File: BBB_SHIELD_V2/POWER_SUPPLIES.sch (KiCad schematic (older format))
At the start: 16 parts, among them P12V1 VX78XX, P5V1 VX78XX

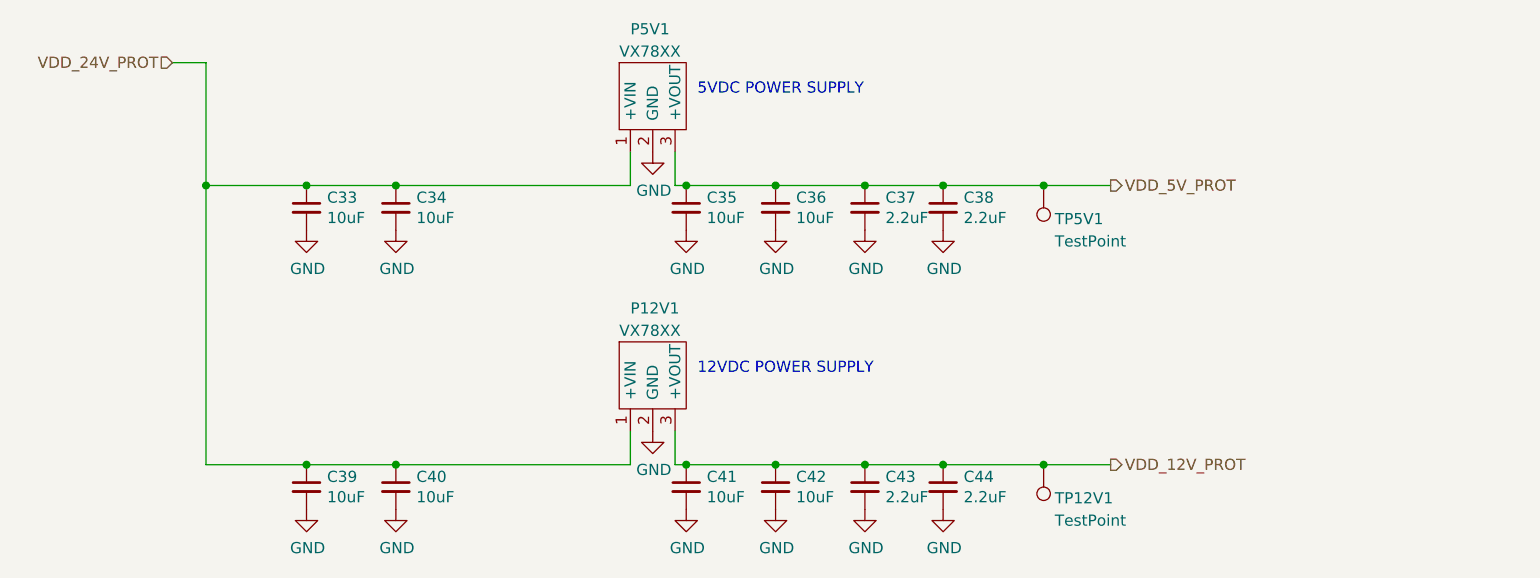
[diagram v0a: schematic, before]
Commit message: Cleaned up schematic.
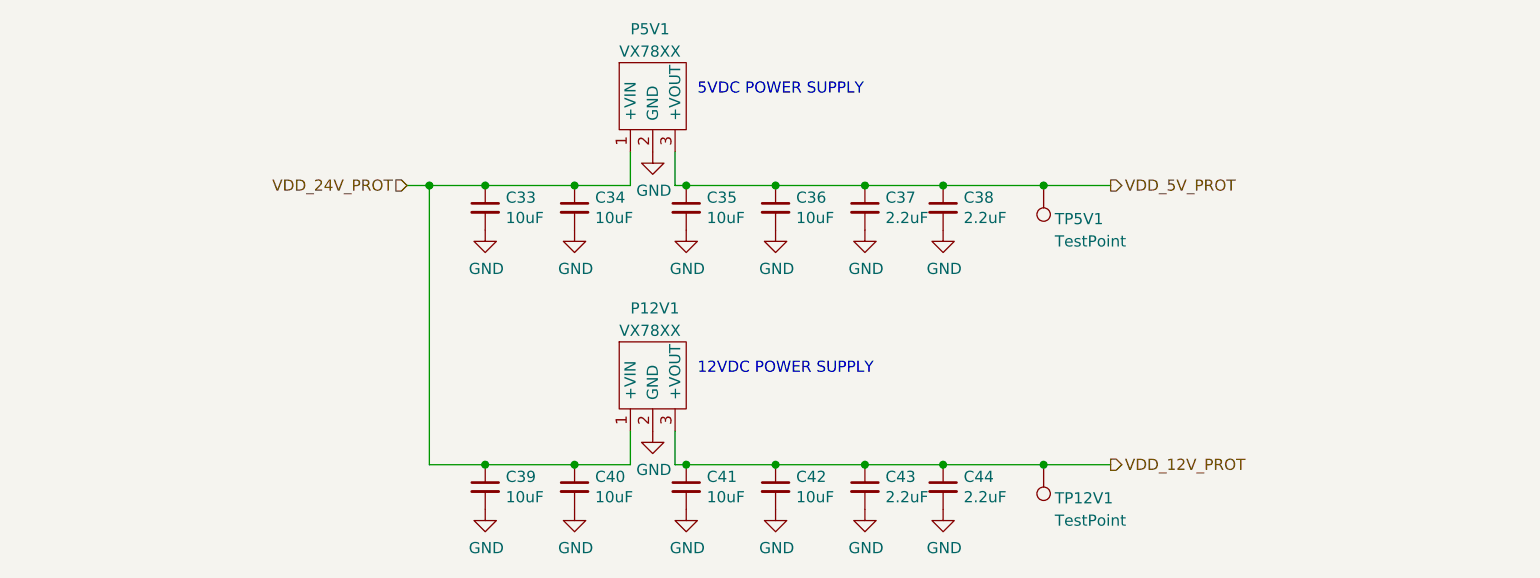
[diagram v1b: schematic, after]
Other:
- moved on the sheet: C33, C34, C39, C40
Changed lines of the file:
@@
 	1    0    0    -1
 $EndComp
-Text HLabel 1800 2200 0    50   Input ~ 0
+Text HLabel 2850 2750 0    50   Input ~ 0
 VDD_24V_PROT
 Text HLabel 6000 2750 2    50   Output ~ 0
@@
 	3850 2600 3850 2750
 Wire Wire Line
-	1950 2750 1950 2200
-Wire Wire Line
-	1950 2200 1800 2200
-Wire Wire Line
 	3850 3850 3850 4000
-Wire Wire Line
-	1950 4000 1950 2750
-Connection ~ 1950 2750
 $Comp
 L power:GND #PWR058
@@
 L Device:C_Small C33
 U 1 1 5C3C2F7D
-P 2400 2850
-F 0 "C33" H 2492 2896 50  0000 L CNN
-F 1 "10uF" H 2492 2805 50  0000 L CNN
-F 2 "Capacitor_SMD:C_1206_3216Metric" H 2400 2850 50  0001 C CNN
-F 3 "~" H 2400 2850 50  0001 C CNN
-F 4 "1276-6736-1-ND" H 2400 2850 50  0001 C CNN "DKPN"
-F 5 "CL31A106MBHNNNE" H 2400 2850 50  0001 C CNN "MFGPN"
-F 6 "X5R" H 2400 2850 50  0001 C CNN "TCO"
-F 7 "50" H 2400 2850 50  0001 C CNN "VOLTAGE"
-	1    2400 2850
-	1    0    0    -1
-$EndComp
-Connection ~ 2400 2750
-Wire Wire Line
-	2400 2750 1950 2750
+P 3200 2850
+F 0 "C33" H 3292 2896 50  0000 L CNN
+F 1 "10uF" H 3292 2805 50  0000 L CNN
+F 2 "Capacitor_SMD:C_1206_3216Metric" H 3200 2850 50  0001 C CNN
+F 3 "~" H 3200 2850 50  0001 C CNN
+F 4 "1276-6736-1-ND" H 3200 2850 50  0001 C CNN "DKPN"
+F 5 "CL31A106MBHNNNE" H 3200 2850 50  0001 C CNN "MFGPN"
+F 6 "X5R" H 3200 2850 50  0001 C CNN "TCO"
+F 7 "50" H 3200 2850 50  0001 C CNN "VOLTAGE"
+	1    3200 2850
+	1    0    0    -1
+$EndComp
 $Comp
 L power:GND #PWR056
 U 1 1 5C3C3A06
-P 2400 2950
-F 0 "#PWR056" H 2400 2700 50  0001 C CNN
-F 1 "GND" H 2405 2777 50  0000 C CNN
-F 2 "" H 2400 2950 50  0001 C CNN
-F 3 "" H 2400 2950 50  0001 C CNN
-	1    2400 2950
+P 3200 2950
+F 0 "#PWR056" H 3200 2700 50  0001 C CNN
+F 1 "GND" H 3205 2777 50  0000 C CNN
+F 2 "" H 3200 2950 50  0001 C CNN
+F 3 "" H 3200 2950 50  0001 C CNN
+	1    3200 2950
 	1    0    0    -1
 $EndComp
@@
 L power:GND #PWR057
 U 1 1 5C3C3A58
-P 2800 2950
-F 0 "#PWR057" H 2800 2700 50  0001 C CNN
-F 1 "GND" H 2805 2777 50  0000 C CNN
-F 2 "" H 2800 2950 50  0001 C CNN
-F 3 "" H 2800 2950 50  0001 C CNN
-	1    2800 2950
+P 3600 2950
+F 0 "#PWR057" H 3600 2700 50  0001 C CNN
+F 1 "GND" H 3605 2777 50  0000 C CNN
+F 2 "" H 3600 2950 50  0001 C CNN
+F 3 "" H 3600 2950 50  0001 C CNN
+	1    3600 2950
 	1    0    0    -1
 $EndComp
@@
 L power:GND #PWR063
 U 1 1 5C3C3AE4
-P 2400 4200
-F 0 "#PWR063" H 2400 3950 50  0001 C CNN
-F 1 "GND" H 2405 4027 50  0000 C CNN
-F 2 "" H 2400 4200 50  0001 C CNN
-F 3 "" H 2400 4200 50  0001 C CNN
-	1    2400 4200
+P 3200 4200
+F 0 "#PWR063" H 3200 3950 50  0001 C CNN
+F 1 "GND" H 3205 4027 50  0000 C CNN
+F 2 "" H 3200 4200 50  0001 C CNN
+F 3 "" H 3200 4200 50  0001 C CNN
+	1    3200 4200
 	1    0    0    -1
 $EndComp
@@
 L power:GND #PWR064
 U 1 1 5C3C3B36
-P 2800 4200
-F 0 "#PWR064" H 2800 3950 50  0001 C CNN
-F 1 "GND" H 2805 4027 50  0000 C CNN
-F 2 "" H 2800 4200 50  0001 C CNN
-F 3 "" H 2800 4200 50  0001 C CNN
-	1    2800 4200
+P 3600 4200
+F 0 "#PWR064" H 3600 3950 50  0001 C CNN
+F 1 "GND" H 3605 4027 50  0000 C CNN
+F 2 "" H 3600 4200 50  0001 C CNN
+F 3 "" H 3600 4200 50  0001 C CNN
+	1    3600 4200
 	1    0    0    -1
 $EndComp
@@
 	5250 4000 5700 4000
 Wire Wire Line
-	2400 2750 2800 2750
-Wire Wire Line
 	4050 2750 4100 2750
 Wire Wire Line
 	4050 4000 4100 4000
-Wire Wire Line
-	1950 4000 2400 4000
 $Comp
 L Device:C_Small C34
 U 1 1 5D1133B6
-P 2800 2850
-F 0 "C34" H 2892 2896 50  0000 L CNN
-F 1 "10uF" H 2892 2805 50  0000 L CNN
-F 2 "Capacitor_SMD:C_1206_3216Metric" H 2800 2850 50  0001 C CNN
-F 3 "~" H 2800 2850 50  0001 C CNN
-F 4 "1276-6736-1-ND" H 2800 2850 50  0001 C CNN "DKPN"
-F 5 "CL31A106MBHNNNE" H 2800 2850 50  0001 C CNN "MFGPN"
-F 6 "X5R" H 2800 2850 50  0001 C CNN "TCO"
-F 7 "50" H 2800 2850 50  0001 C CNN "VOLTAGE"
-	1    2800 2850
+P 3600 2850
+F 0 "C34" H 3692 2896 50  0000 L CNN
+F 1 "10uF" H 3692 2805 50  0000 L CNN
+F 2 "Capacitor_SMD:C_1206_3216Metric" H 3600 2850 50  0001 C CNN
+F 3 "~" H 3600 2850 50  0001 C CNN
+F 4 "1276-6736-1-ND" H 3600 2850 50  0001 C CNN "DKPN"
+F 5 "CL31A106MBHNNNE" H 3600 2850 50  0001 C CNN "MFGPN"
+F 6 "X5R" H 3600 2850 50  0001 C CNN "TCO"
+F 7 "50" H 3600 2850 50  0001 C CNN "VOLTAGE"
+	1    3600 2850
 	1    0    0    -1
 $EndComp
@@
 L Device:C_Small C39
 U 1 1 5D1136C3
-P 2400 4100
-F 0 "C39" H 2492 4146 50  0000 L CNN
-F 1 "10uF" H 2492 4055 50  0000 L CNN
-F 2 "Capacitor_SMD:C_1206_3216Metric" H 2400 4100 50  0001 C CNN
-F 3 "~" H 2400 4100 50  0001 C CNN
-F 4 "1276-6736-1-ND" H 2400 4100 50  0001 C CNN "DKPN"
-F 5 "CL31A106MBHNNNE" H 2400 4100 50  0001 C CNN "MFGPN"
-F 6 "X5R" H 2400 4100 50  0001 C CNN "TCO"
-F 7 "50" H 2400 4100 50  0001 C CNN "VOLTAGE"
-	1    2400 4100
+P 3200 4100
+F 0 "C39" H 3292 4146 50  0000 L CNN
+F 1 "10uF" H 3292 4055 50  0000 L CNN
+F 2 "Capacitor_SMD:C_1206_3216Metric" H 3200 4100 50  0001 C CNN
+F 3 "~" H 3200 4100 50  0001 C CNN
+F 4 "1276-6736-1-ND" H 3200 4100 50  0001 C CNN "DKPN"
+F 5 "CL31A106MBHNNNE" H 3200 4100 50  0001 C CNN "MFGPN"
+F 6 "X5R" H 3200 4100 50  0001 C CNN "TCO"
+F 7 "50" H 3200 4100 50  0001 C CNN "VOLTAGE"
+	1    3200 4100
 	1    0    0    -1
 $EndComp
@@
 L Device:C_Small C40
 U 1 1 5D1137C0
-P 2800 4100
-F 0 "C40" H 2892 4146 50  0000 L CNN
-F 1 "10uF" H 2892 4055 50  0000 L CNN
-F 2 "Capacitor_SMD:C_1206_3216Metric" H 2800 4100 50  0001 C CNN
-F 3 "~" H 2800 4100 50  0001 C CNN
-F 4 "1276-6736-1-ND" H 2800 4100 50  0001 C CNN "DKPN"
-F 5 "CL31A106MBHNNNE" H 2800 4100 50  0001 C CNN "MFGPN"
-F 6 "X5R" H 2800 4100 50  0001 C CNN "TCO"
-F 7 "50" H 2800 4100 50  0001 C CNN "VOLTAGE"
-	1    2800 4100
+P 3600 4100
+F 0 "C40" H 3692 4146 50  0000 L CNN
+F 1 "10uF" H 3692 4055 50  0000 L CNN
+F 2 "Capacitor_SMD:C_1206_3216Metric" H 3600 4100 50  0001 C CNN
+F 3 "~" H 3600 4100 50  0001 C CNN
+F 4 "1276-6736-1-ND" H 3600 4100 50  0001 C CNN "DKPN"
+F 5 "CL31A106MBHNNNE" H 3600 4100 50  0001 C CNN "MFGPN"
+F 6 "X5R" H 3600 4100 50  0001 C CNN "TCO"
+F 7 "50" H 3600 4100 50  0001 C CNN "VOLTAGE"
+	1    3600 4100
 	1    0    0    -1
 $EndComp
@@
 Wire Wire Line
 	4100 4000 4500 4000
-Connection ~ 2800 4000
-Wire Wire Line
-	2800 4000 3850 4000
-Connection ~ 2400 4000
-Wire Wire Line
-	2400 4000 2800 4000
-Connection ~ 2800 2750
-Wire Wire Line
-	2800 2750 3850 2750
 Connection ~ 4100 2750
 Wire Wire Line
@@
 Wire Wire Line
 	5700 4000 6000 4000
+Wire Wire Line
+	3200 2750 3600 2750
+Connection ~ 3600 2750
+Wire Wire Line
+	3600 2750 3850 2750
+Wire Wire Line
+	3200 4000 3600 4000
+Connection ~ 3600 4000
+Wire Wire Line
+	3600 4000 3850 4000
+Wire Wire Line
+	3200 2750 2950 2750
+Connection ~ 3200 2750
+Wire Wire Line
+	3200 4000 2950 4000
+Connection ~ 3200 4000
+Wire Wire Line
+	2950 2750 2950 4000
+Wire Wire Line
+	2850 2750 2950 2750
+Connection ~ 2950 2750
 $EndSCHEMATC

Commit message: Rev 2 problem fixes.
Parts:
- added C46, C47, C48: 180uF,50V, Capacitor_THT:CP_Radial_D8.0mm_P3.50mm, symbol Device:CP
- C33, C34, C35, C36, C39, C40, C41, C42: DKPN 1276-6736-1-ND -> 1276-6767-1-ND; MFG (none) -> SAMSUNG; MFGPN CL31A106MBHNNNE -> CL31B106KBHNNNE; NOTES (none) -> VER,2019-07-17,CT; TCO X5R -> (none); TEMPCO (none) -> X7R
- C37, C38, C43, C44: MFG (none) -> SAMSUNG; NOTES (none) -> VER,2019-07-17,REEL; TEMPCO (none) -> X5R; VOLTAGE (none) -> 50
- P12V1, P5V1: NOTES (none) -> VER,2019-07-15,BULK
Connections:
- net GND: now also C46.2, C47.2, C48.2
- net VDD_5V_PROT: now also C46.1, C47.1, C48.1
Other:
- moved on the sheet: TP12V1, TP5V1
